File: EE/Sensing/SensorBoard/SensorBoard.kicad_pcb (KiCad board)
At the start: 2 copper layers, 40 x 76.5 mm, 123 parts, among them J1 Conn_01x04_Male, J101 Peg, J102 Peg, J11 Peg, J12 Peg, J21 Peg, J22 Peg, J31 Peg, J32 Peg, J41 Peg, J42 Peg, J51 Peg, J52 Peg, J61 Peg, J62 Peg, J71 Peg, J72 Peg, J81 Peg, J82 Peg, J91 Peg, J92 Peg, Q1 BSS84DW, Q10 BSS84DW, Q11 DMP31D1U-7, Q12 DMP31D1U-7, Q2 BSS84DW, Q3 BSS84DW, Q4 BSS84DW, Q5 BSS84DW, Q6 BSS84DW, Q7 BSS84DW, Q8 BSS84DW, Q9 BSS84DW, U1 TCR2EE27, U101 AH1381, U102 AH1381, U11 AH1381, U12 AH1381, U2 TCR2EE32, U21 AH1381, U22 AH1381, U3 TCA9555PWR, U31 AH1381, U32 AH1381, U41 AH1381, U42 AH1381, U51 AH1381, U52 AH1381, U61 AH1381, U62 AH1381, U71 AH1381, U72 AH1381, U81 AH1381, U82 AH1381, U91 AH1381, U92 AH1381

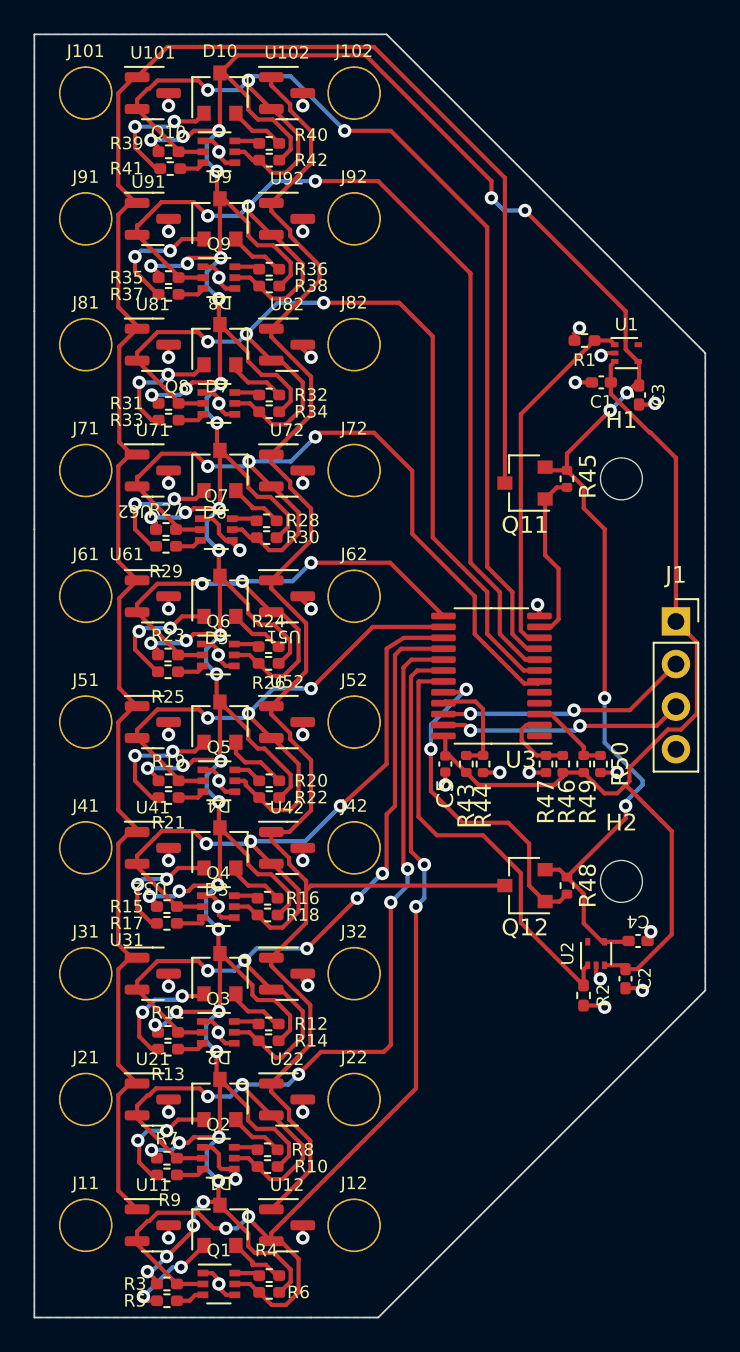
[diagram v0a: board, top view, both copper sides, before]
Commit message: Fixed Silkscreens
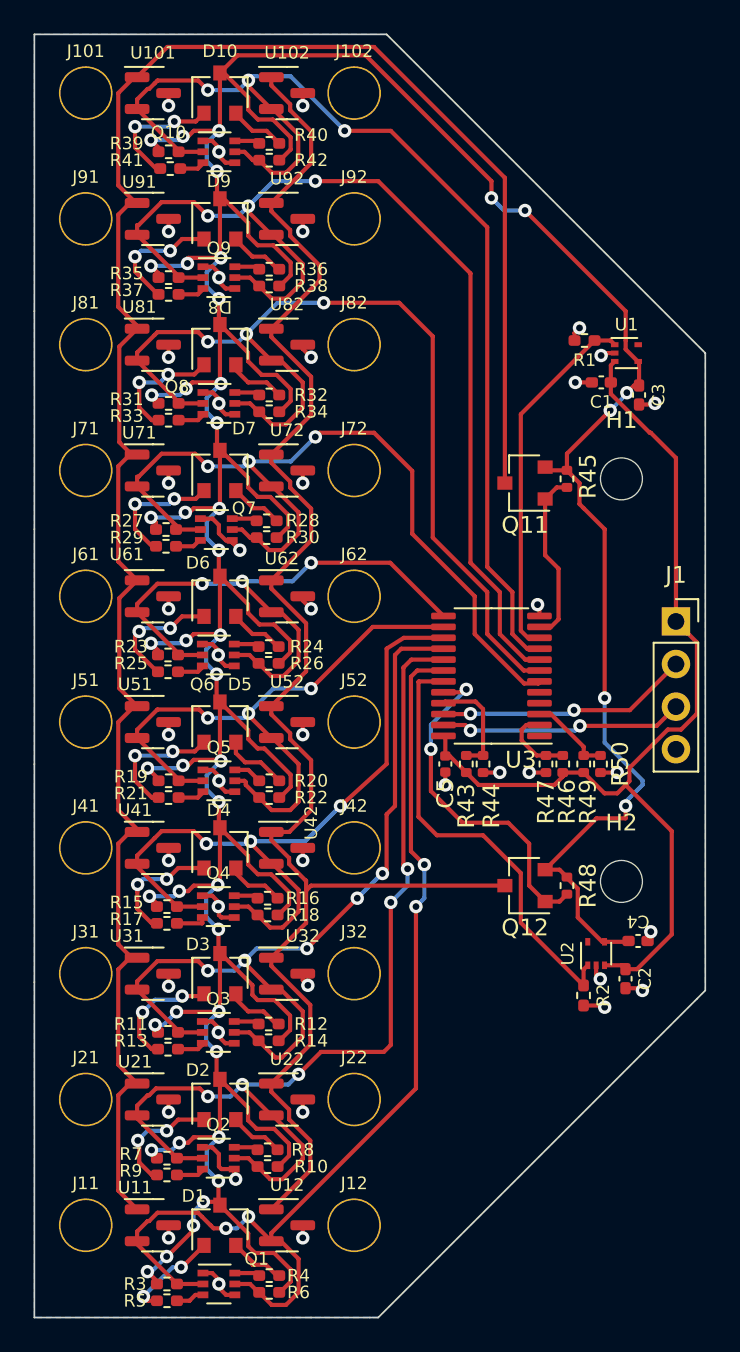
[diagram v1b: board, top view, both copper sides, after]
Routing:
- net /2v7: track 286.8 -> 288.0 mm

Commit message: Updated layout, and placement for main board
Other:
- outline, holes or cut-outs redrawn
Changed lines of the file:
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@@
   (gr_line (start 218 48.5) (end 218 35.5) (layer "Edge.Cuts") (width 0.1))
   (gr_line (start 218 95.5) (end 218 75.5) (layer "Edge.Cuts") (width 0.1))
-  (gr_line (start 238.5 95.5) (end 257.5 76.5) (layer "Edge.Cuts") (width 0.1))
+  (gr_line (start 238.5 95.5) (end 258 76) (layer "Edge.Cuts") (width 0.1))
   (gr_line (start 234.5 95.5) (end 238 95.5) (layer "Edge.Cuts") (width 0.1))
   (gr_line (start 258 38) (end 239 19) (layer "Edge.Cuts") (width 0.1))
-  (gr_line (start 258 76) (end 257.5 76.5) (layer "Edge.Cuts") (width 0.1))
   (gr_line (start 238 95.5) (end 238.5 95.5) (layer "Edge.Cuts") (width 0.1))
   (gr_line (start 218 48.5) (end 218 62.5) (layer "Edge.Cuts") (width 0.1))

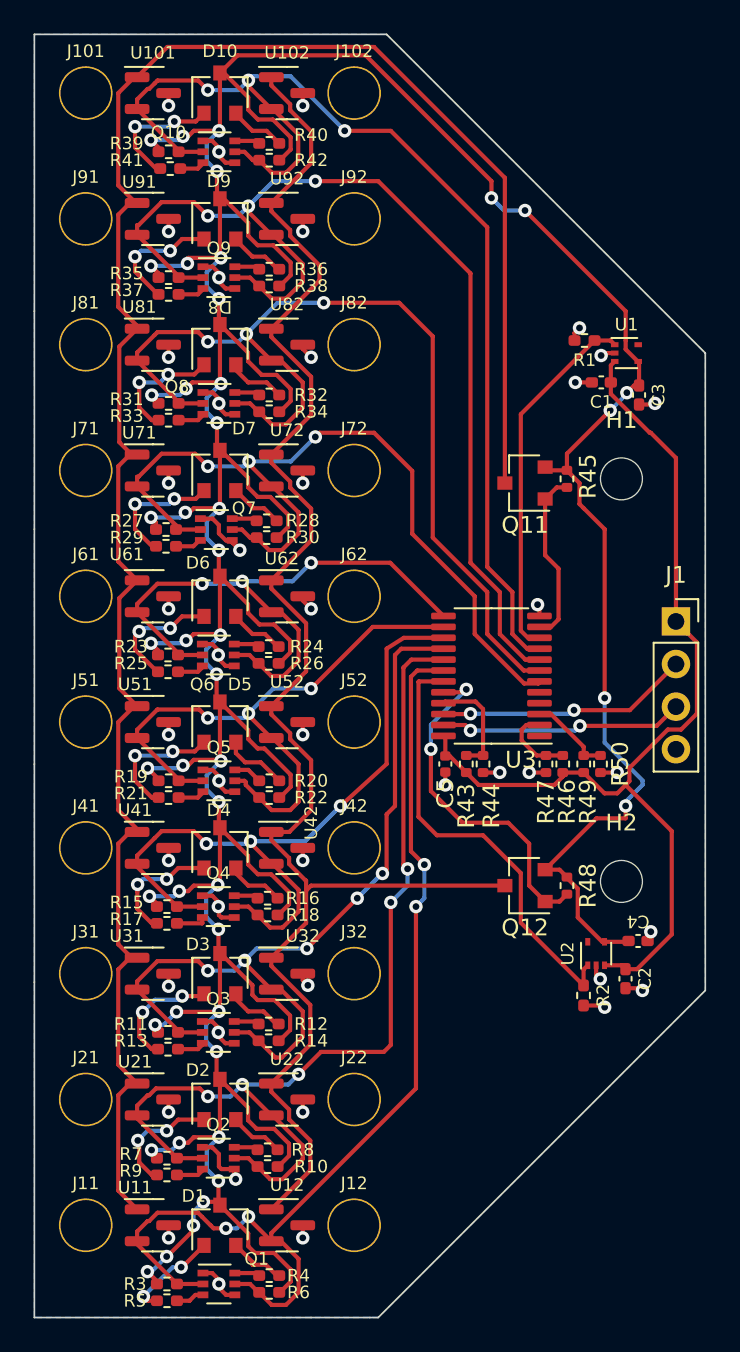
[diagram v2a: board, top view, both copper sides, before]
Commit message: Replacement after sensing change
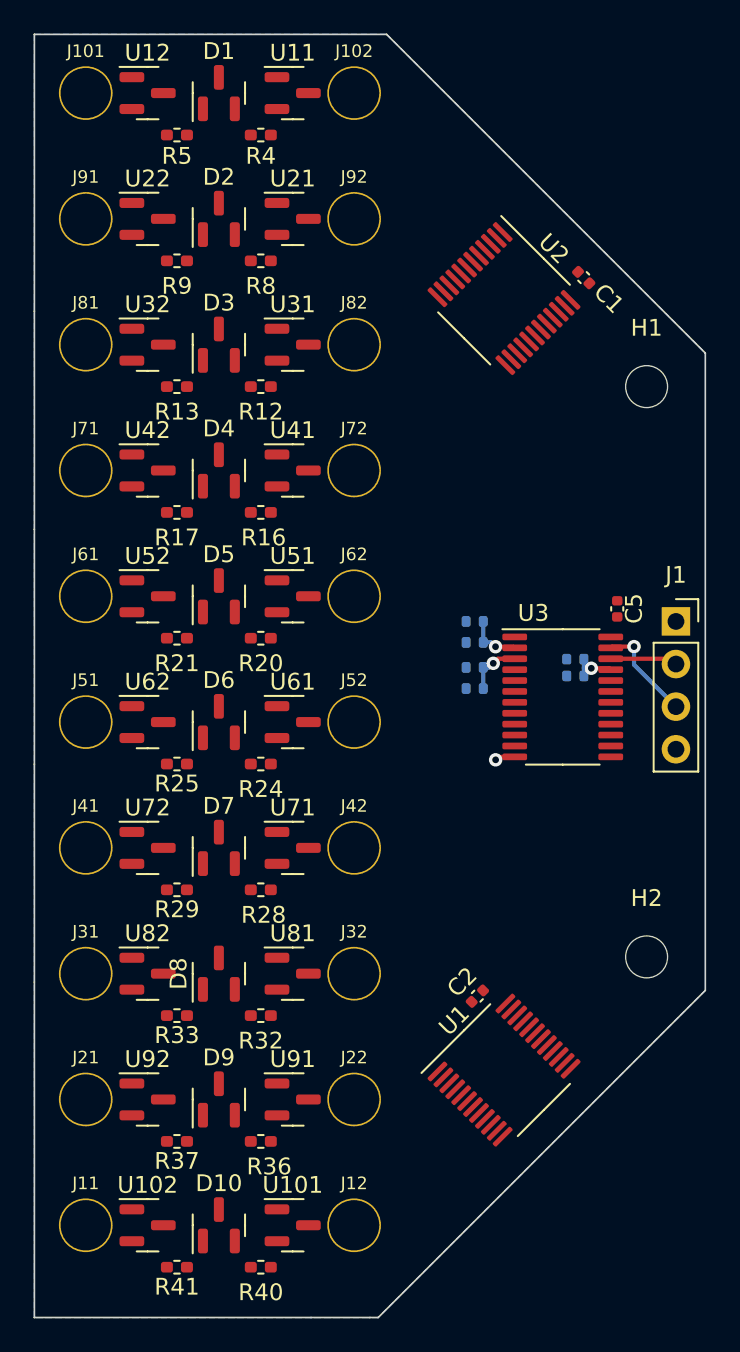
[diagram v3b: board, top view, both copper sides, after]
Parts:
- removed C3, C4: 0.1u, Capacitor_SMD:C_0402_1005Metric_Pad0.74x0.62mm_HandSolder
- removed Q1, Q10, Q2, Q3, Q4, Q5, Q6, Q7, Q8, Q9: BSS84DW, Package_TO_SOT_SMD:SOT-363_SC-70-6
- removed Q11, Q12: DMP31D1U-7, Package_TO_SOT_SMD:SC-59
- removed R1, R2: 100k, Resistor_SMD:R_0402_1005Metric_Pad0.72x0.64mm_HandSolder
- removed R10, R11, R14, R15, R18, R19, R22, R23, R26, R27, R3, R30, R31, R34, R35, R38, R39, R42, R6, R7: 100k_NP, Resistor_SMD:R_0402_1005Metric_Pad0.72x0.64mm_HandSolder
- removed R45, R48: 10k, Resistor_SMD:R_0402_1005Metric
- C1, C2: footprint Capacitor_SMD:C_0402_1005Metric_Pad0.74x0.62mm_HandSolder -> Capacitor_SMD:C_0402_1005Metric
- D1, D10, D2, D3, D4, D5, D6, D7, D8, D9: footprint Package_TO_SOT_SMD:SC-59 -> Package_TO_SOT_SMD:SOT-23
- R24, R25: value 500 -> 560
- R43, R44, R46, R47, R49, R50: moved to B.Cu
- U1: value TCR2EE27 -> SN74LVC827APWR; footprint Package_TO_SOT_SMD:SOT-553 -> Package_SO:TSSOP-24_4.4x6.5mm_P0.5mm
- U101, U102, U11, U12, U21, U22, U31, U32, U41, U42, U51, U52, U61, U62, U71, U72, U81, U82, U91, U92: value AH1381 -> DRV5032AJDBZR
- U2: value TCR2EE32 -> SN74LVC827APWR; footprint Package_TO_SOT_SMD:SOT-553 -> Package_SO:TSSOP-24_4.4x6.5mm_P0.5mm
- moved R5 69.5 mm to (226.5, 25.0), turned to 180 degrees
- moved U101 68.0 mm to (233.4, 90.0)
- moved U11 68.0 mm to (233.4, 22.5)
- moved U102 68.0 mm to (224.8, 90.0)
- moved U12 68.0 mm to (224.8, 22.5)
- moved R4 68.0 mm to (231.5, 25.0), turned to 0 degrees
- moved D1 67.5 mm to (229.0, 22.5)
- moved D10 67.5 mm to (229.0, 90.0)
- moved R40 67.0 mm to (231.5, 92.5), turned to 0 degrees
- moved R41 65.5 mm to (226.5, 92.5), turned to 180 degrees
- moved R9 54.5 mm to (226.5, 32.5), turned to 180 degrees
- moved U21 53.2 mm to (233.4, 30.0)
- moved U91 53.2 mm to (233.4, 82.5)
- moved U22 53.2 mm to (224.8, 30.0)
- moved U92 53.2 mm to (224.8, 82.5)
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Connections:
- D1 pad 3: /2v7 -> VCC
- D10 pad 3: /2v7 -> VCC
- D2 pad 3: /2v7 -> VCC
- D3 pad 3: /2v7 -> VCC
- D4 pad 3: /2v7 -> VCC
- D5 pad 3: /2v7 -> VCC
- D6 pad 3: /2v7 -> VCC
- D7 pad 3: /2v7 -> VCC
- D8 pad 3: /2v7 -> VCC
- D9 pad 3: /2v7 -> VCC
- R12 pad 2: Net-(Q3-Pad6) -> /B02
- R13 pad 2: Net-(Q3-Pad3) -> /B07
- R16 pad 2: Net-(Q4-Pad6) -> /B03
- R17 pad 2: Net-(Q4-Pad3) -> /B08
- R20 pad 2: Net-(Q5-Pad6) -> /B04
- R21 pad 2: Net-(Q5-Pad3) -> /B09
- R24 pad 2: Net-(Q6-Pad6) -> /B10
- R25 pad 2: Net-(Q6-Pad3) -> /B15
- R28 pad 2: Net-(Q7-Pad6) -> /B11
- R29 pad 2: Net-(Q7-Pad3) -> /B16
- R32 pad 2: Net-(Q8-Pad6) -> /B12
- R33 pad 2: Net-(Q8-Pad3) -> /B17
- R36 pad 2: Net-(Q9-Pad6) -> /B13
- R37 pad 2: Net-(Q9-Pad3) -> /B18
- R4 pad 2: Net-(Q1-Pad6) -> /B00
- R40 pad 2: Net-(Q10-Pad6) -> /B14
- R41 pad 2: Net-(Q10-Pad3) -> /B19
- R5 pad 2: Net-(Q1-Pad3) -> /B05
- R8 pad 2: Net-(Q2-Pad6) -> /B01
- R9 pad 2: Net-(Q2-Pad3) -> /B06
- U1 pad 1: /2v7_EN -> /B1Select
- U1 pad 2: GND -> /B10
- U1 pad 3: VCC -> /B11
- U1 pad 4: /2v7 -> /B12
- U1 pad 5: unconnected-(U1-Pad5) -> /B13
- U101 pad 1: /VCC0 -> VCC
- U102 pad 1: /VCC1 -> VCC
- U102 pad 2: /B14 -> /B19
- U11 pad 1: /VCC0 -> VCC
- U12 pad 1: /VCC1 -> VCC
- U12 pad 2: /B00 -> /B05
- U2 pad 1: /3v2_EN -> /B0Select
- U2 pad 2: GND -> /B00
- U2 pad 3: VCC -> /B01
- U2 pad 4: /2v7 -> /B02
- U2 pad 5: unconnected-(U2-Pad5) -> /B03
- U21 pad 1: /VCC0 -> VCC
- U22 pad 1: /VCC1 -> VCC
- U22 pad 2: /B01 -> /B06
- U3 pad 10: /2v7_EN -> /Out6
- U3 pad 11: /B0_EN -> /Out7
- U3 pad 13: /B10 -> unconnected-(U3-Pad13)
- U3 pad 14: /B04 -> /Out8
- U3 pad 15: /B03 -> /Out9
- U3 pad 16: /B02 -> unconnected-(U3-Pad16)
- U3 pad 17: /B01 -> unconnected-(U3-Pad17)
- U3 pad 18: /B00 -> unconnected-(U3-Pad18)
- U3 pad 19: /3v2_EN -> unconnected-(U3-Pad19)
- U3 pad 20: /B1_EN -> unconnected-(U3-Pad20)
- U3 pad 4: unconnected-(U3-Pad4) -> /Out0
- U3 pad 5: unconnected-(U3-Pad5) -> /Out1
- U3 pad 6: /B11 -> /Out2
- U3 pad 7: /B12 -> /Out3
- U3 pad 8: /B13 -> /Out4
- U3 pad 9: /B14 -> /Out5
- U31 pad 1: /VCC0 -> VCC
- U32 pad 1: /VCC1 -> VCC
- U32 pad 2: /B02 -> /B07
- U41 pad 1: /VCC0 -> VCC
- U42 pad 1: /VCC1 -> VCC
- U42 pad 2: /B03 -> /B08
- U51 pad 1: /VCC0 -> VCC
- U52 pad 1: /VCC1 -> VCC
- U52 pad 2: /B04 -> /B09
- U61 pad 1: /VCC0 -> VCC
- U62 pad 1: /VCC1 -> VCC
- U62 pad 2: /B10 -> /B15
- U71 pad 1: /VCC0 -> VCC
- U72 pad 1: /VCC1 -> VCC
- U72 pad 2: /B11 -> /B16
- U81 pad 1: /VCC0 -> VCC
- U82 pad 1: /VCC1 -> VCC
- U82 pad 2: /B12 -> /B17
- U91 pad 1: /VCC0 -> VCC
- U92 pad 1: /VCC1 -> VCC
- U92 pad 2: /B13 -> /B18
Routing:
- net /2v7: track 288.0 -> 0.00 mm, vias 46 -> 0
- net /VCC0: track 121.8 -> 0.00 mm
- net /VCC1: track 97.7 -> 0.00 mm
- net /B14: track 68.8 -> 0.00 mm, vias 3 -> 0
- net /B13: track 65.7 -> 0.00 mm, vias 3 -> 0
- net /B00: track 64.0 -> 0.00 mm, vias 4 -> 0
- net /B12: track 59.9 -> 0.00 mm, vias 3 -> 0
- net /B01: track 59.3 -> 0.00 mm, vias 5 -> 0
- net VCC: track 58.6 -> 0.00 mm
- net GND: track 56.7 -> 1.21 mm, vias 43 -> 1
- net /B11: track 51.5 -> 0.00 mm, vias 3 -> 0
- net /B02: track 51.2 -> 0.00 mm, vias 5 -> 0
- net /B03: track 43.8 -> 0.00 mm, vias 3 -> 0
- net /B04: track 38.1 -> 0.00 mm, vias 3 -> 0
- net /B10: track 37.3 -> 0.00 mm, vias 3 -> 0
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
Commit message: Potential Layout - Inverted 1 chip for layout
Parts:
- moved C1 2.66 mm to (251.9, 35.9), turned to -45 degrees
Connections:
- U1 pad 10: /B18 -> /B14
- U1 pad 2: /B10 -> /B15
- U1 pad 3: /B11 -> /B10
- U1 pad 4: /B12 -> /B11
- U1 pad 5: /B13 -> /B16
- U1 pad 6: /B14 -> /B12
- U1 pad 7: /B15 -> /B17
- U1 pad 8: /B16 -> /B13
- U1 pad 9: /B17 -> /B18
- U2 pad 10: /B08 -> /B09
- U2 pad 11: /B09 -> /B04
- U2 pad 14: /Out9 -> /Out0
- U2 pad 15: /Out8 -> /Out1
- U2 pad 16: /Out7 -> /Out2
- U2 pad 17: /Out6 -> /Out3
- U2 pad 18: /Out5 -> /Out4
- U2 pad 19: /Out4 -> /Out5
- U2 pad 20: /Out3 -> /Out6
- U2 pad 21: /Out2 -> /Out7
- U2 pad 22: /Out1 -> /Out8
- U2 pad 23: /Out0 -> /Out9
- U2 pad 3: /B01 -> /B05
- U2 pad 4: /B02 -> /B01
- U2 pad 5: /B03 -> /B06
- U2 pad 6: /B04 -> /B02
- U2 pad 7: /B05 -> /B07
- U2 pad 8: /B06 -> /B03
- U2 pad 9: /B07 -> /B08
- U3 pad 13: unconnected-(U3-Pad13) -> /Out9
- U3 pad 15: /Out9 -> /B1Select
- U3 pad 19: unconnected-(U3-Pad19) -> /B0Select
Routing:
- net VCC: track 0.00 -> 365.1 mm, vias 0 -> 5
- net /Out9: track 0.00 -> 52.7 mm, vias 0 -> 4
- net /Out8: track 0.00 -> 51.6 mm, vias 0 -> 2
- net /Out6: track 0.00 -> 50.5 mm
- net /Out5: track 0.00 -> 50.1 mm
- net /Out4: track 0.00 -> 49.9 mm
- net /Out7: track 0.00 -> 49.8 mm, vias 0 -> 2
- net /Out3: track 0.00 -> 49.7 mm
- net /Out2: track 0.00 -> 49.2 mm
- net /Out1: track 0.00 -> 48.7 mm
- net /Out0: track 0.00 -> 48.1 mm
- net /B0Select: track 0.00 -> 44.7 mm, vias 0 -> 4
- net /B09: track 0.00 -> 40.1 mm
- net GND: track 1.21 -> 37.7 mm, vias 1 -> 26
- net /B15: track 0.00 -> 35.5 mm
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
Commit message: Routine Update
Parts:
- U1, U2: footprint Package_SO:TSSOP-24_4.4x6.5mm_P0.5mm -> Package_SO:TSSOP-24_4.4x7.8mm_P0.65mm
- moved U1 0.81 mm to (246.8, 81.0)
- moved C1 0.45 mm to (252.3, 35.7)
- moved U2 0.18 mm to (246.1, 34.9)
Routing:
- net VCC: track 365.1 -> 334.2 mm, vias 5 -> 9
- net /B1Select: track 35.3 -> 40.5 mm, vias 2 -> 4
- net /B0Select: track 44.7 -> 48.3 mm, vias 4 -> 2
- net /B02: track 24.1 -> 20.7 mm
- net /B06: track 26.1 -> 22.7 mm
- net /B01: track 19.0 -> 15.7 mm
- net /Out0: track 48.1 -> 47.0 mm
- net /B04: track 31.0 -> 29.9 mm
- net /Out1: track 48.7 -> 47.7 mm
- net /B03: track 27.3 -> 26.4 mm
- net /B18: track 23.1 -> 23.9 mm
- net /B09: track 40.1 -> 39.3 mm
- net /Out7: track 49.8 -> 50.5 mm
- net /B13: track 15.1 -> 15.8 mm
- net /B07: track 28.7 -> 28.0 mm
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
